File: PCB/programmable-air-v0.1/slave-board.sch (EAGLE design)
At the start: 16 parts, among them Q1 600mA/40V, Q2 600mA/40V, Q3 600mA/40V

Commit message: Forgot to add 5V input to slave boards
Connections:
- net GND: no longer U$5.P$2, U$6.P$2, U$7.P$2
- net N$7: now also U$7.P$2; no longer U$7.P$1
- net N$8: now also U$6.P$2; no longer U$6.P$1
- net N$9: now also U$5.P$2; no longer U$5.P$1
- net VIN: now also U$5.P$1, U$6.P$1, U$7.P$1
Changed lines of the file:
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@@
 <instance part="R2" gate="G$1" x="-11.43" y="-16.51"/>
 <instance part="R3" gate="G$1" x="21.59" y="-16.51"/>
-<instance part="U$5" gate="G$1" x="-29.21" y="-16.51" rot="R90"/>
-<instance part="U$6" gate="G$1" x="3.81" y="-16.51" rot="R90"/>
-<instance part="U$7" gate="G$1" x="36.83" y="-16.51" rot="R90"/>
+<instance part="U$5" gate="G$1" x="-33.02" y="-6.35" rot="R180"/>
+<instance part="U$6" gate="G$1" x="0" y="-6.35" rot="R180"/>
+<instance part="U$7" gate="G$1" x="33.02" y="-7.62" rot="R180"/>
 <instance part="SUPPLY1" gate="G$1" x="-48.26" y="35.56"/>
 <instance part="GND1" gate="1" x="13.97" y="-24.13"/>
@@
 <net name="N$7" class="0">
 <segment>
-<pinref part="U$7" gate="G$1" pin="P$1"/>
 <pinref part="Q3" gate="G$1" pin="C"/>
-<wire x1="36.83" y1="-13.97" x2="36.83" y2="-11.43" width="0.1524" layer="91"/>
-<wire x1="36.83" y1="-11.43" x2="33.02" y2="-11.43" width="0.1524" layer="91"/>
-<wire x1="36.83" y1="-11.43" x2="48.26" y2="-11.43" width="0.1524" layer="91"/>
+<wire x1="33.02" y1="-11.43" x2="48.26" y2="-11.43" width="0.1524" layer="91"/>
 <pinref part="U$4" gate="G$1" pin="P$2"/>
 <wire x1="48.26" y1="-11.43" x2="48.26" y2="-10.16" width="0.1524" layer="91"/>
+<pinref part="U$7" gate="G$1" pin="P$2"/>
+<wire x1="35.56" y1="-7.62" x2="48.26" y2="-7.62" width="0.1524" layer="91"/>
+<wire x1="48.26" y1="-7.62" x2="48.26" y2="-10.16" width="0.1524" layer="91"/>
 </segment>
 </net>
 <net name="N$8" class="0">
 <segment>
-<pinref part="U$6" gate="G$1" pin="P$1"/>
-<wire x1="3.81" y1="-13.97" x2="3.81" y2="-11.43" width="0.1524" layer="91"/>
 <pinref part="Q2" gate="G$1" pin="C"/>
-<wire x1="3.81" y1="-11.43" x2="0" y2="-11.43" width="0.1524" layer="91"/>
-<wire x1="3.81" y1="-11.43" x2="15.24" y2="-11.43" width="0.1524" layer="91"/>
+<wire x1="0" y1="-11.43" x2="15.24" y2="-11.43" width="0.1524" layer="91"/>
 <pinref part="U$3" gate="G$1" pin="P$2"/>
 <wire x1="15.24" y1="-11.43" x2="15.24" y2="-10.16" width="0.1524" layer="91"/>
+<pinref part="U$6" gate="G$1" pin="P$2"/>
+<wire x1="2.54" y1="-6.35" x2="15.24" y2="-6.35" width="0.1524" layer="91"/>
+<wire x1="15.24" y1="-6.35" x2="15.24" y2="-10.16" width="0.1524" layer="91"/>
 </segment>
 </net>
@@
 <segment>
 <pinref part="Q1" gate="G$1" pin="C"/>
-<wire x1="-33.02" y1="-11.43" x2="-29.21" y2="-11.43" width="0.1524" layer="91"/>
-<pinref part="U$5" gate="G$1" pin="P$1"/>
-<wire x1="-29.21" y1="-11.43" x2="-29.21" y2="-13.97" width="0.1524" layer="91"/>
 <pinref part="U$2" gate="G$1" pin="P$2"/>
 <wire x1="-17.78" y1="-10.16" x2="-17.78" y2="-11.43" width="0.1524" layer="91"/>
-<wire x1="-17.78" y1="-11.43" x2="-29.21" y2="-11.43" width="0.1524" layer="91"/>
+<wire x1="-17.78" y1="-11.43" x2="-33.02" y2="-11.43" width="0.1524" layer="91"/>
+<pinref part="U$5" gate="G$1" pin="P$2"/>
+<wire x1="-30.48" y1="-6.35" x2="-17.78" y2="-6.35" width="0.1524" layer="91"/>
+<wire x1="-17.78" y1="-6.35" x2="-17.78" y2="-10.16" width="0.1524" layer="91"/>
 </segment>
 </net>
@@
 <wire x1="-15.24" y1="-8.89" x2="17.78" y2="-8.89" width="0.1524" layer="91"/>
 <wire x1="17.78" y1="-8.89" x2="17.78" y2="-10.16" width="0.1524" layer="91"/>
-<wire x1="-48.26" y1="35.56" x2="-48.26" y2="-8.89" width="0.1524" layer="91"/>
+<wire x1="-48.26" y1="35.56" x2="-48.26" y2="-6.35" width="0.1524" layer="91"/>
 <pinref part="SUPPLY1" gate="G$1" pin="VIN"/>
 <junction x="-48.26" y="35.56"/>
+<pinref part="U$5" gate="G$1" pin="P$1"/>
+<wire x1="-48.26" y1="-6.35" x2="-48.26" y2="-8.89" width="0.1524" layer="91"/>
+<wire x1="-48.26" y1="-6.35" x2="-35.56" y2="-6.35" width="0.1524" layer="91"/>
+<wire x1="-15.24" y1="-8.89" x2="-15.24" y2="-6.35" width="0.1524" layer="91"/>
+<pinref part="U$6" gate="G$1" pin="P$1"/>
+<wire x1="-15.24" y1="-6.35" x2="-2.54" y2="-6.35" width="0.1524" layer="91"/>
+<wire x1="17.78" y1="-8.89" x2="17.78" y2="-7.62" width="0.1524" layer="91"/>
+<pinref part="U$7" gate="G$1" pin="P$1"/>
+<wire x1="17.78" y1="-7.62" x2="30.48" y2="-7.62" width="0.1524" layer="91"/>
 </segment>
 <segment>
@@
 <segment>
 <pinref part="Q3" gate="G$1" pin="E"/>
-<pinref part="U$7" gate="G$1" pin="P$2"/>
 <wire x1="33.02" y1="-21.59" x2="36.83" y2="-21.59" width="0.1524" layer="91"/>
-<wire x1="36.83" y1="-21.59" x2="36.83" y2="-19.05" width="0.1524" layer="91"/>
 <pinref part="Q2" gate="G$1" pin="E"/>
-<pinref part="U$6" gate="G$1" pin="P$2"/>
-<wire x1="3.81" y1="-21.59" x2="3.81" y2="-19.05" width="0.1524" layer="91"/>
 <wire x1="33.02" y1="-21.59" x2="13.97" y2="-21.59" width="0.1524" layer="91"/>
-<wire x1="13.97" y1="-21.59" x2="3.81" y2="-21.59" width="0.1524" layer="91"/>
-<wire x1="3.81" y1="-21.59" x2="0" y2="-21.59" width="0.1524" layer="91"/>
+<wire x1="13.97" y1="-21.59" x2="0" y2="-21.59" width="0.1524" layer="91"/>
 <pinref part="Q1" gate="G$1" pin="E"/>
-<pinref part="U$5" gate="G$1" pin="P$2"/>
-<wire x1="-33.02" y1="-21.59" x2="-29.21" y2="-21.59" width="0.1524" layer="91"/>
-<wire x1="-29.21" y1="-21.59" x2="-29.21" y2="-19.05" width="0.1524" layer="91"/>
-<wire x1="0" y1="-21.59" x2="-29.21" y2="-21.59" width="0.1524" layer="91"/>
+<wire x1="0" y1="-21.59" x2="-33.02" y2="-21.59" width="0.1524" layer="91"/>
 <pinref part="GND1" gate="1" pin="GND"/>
 <junction x="13.97" y="-21.59"/>

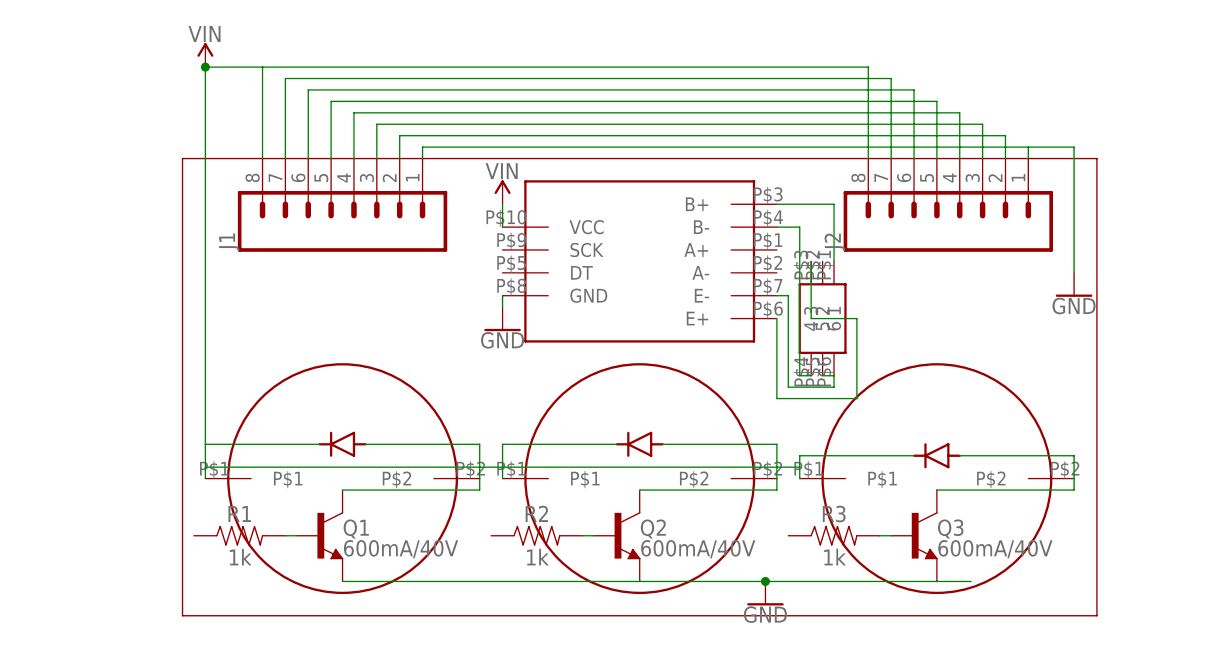
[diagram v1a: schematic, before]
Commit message: Fixed errors found after production, assembly and testing
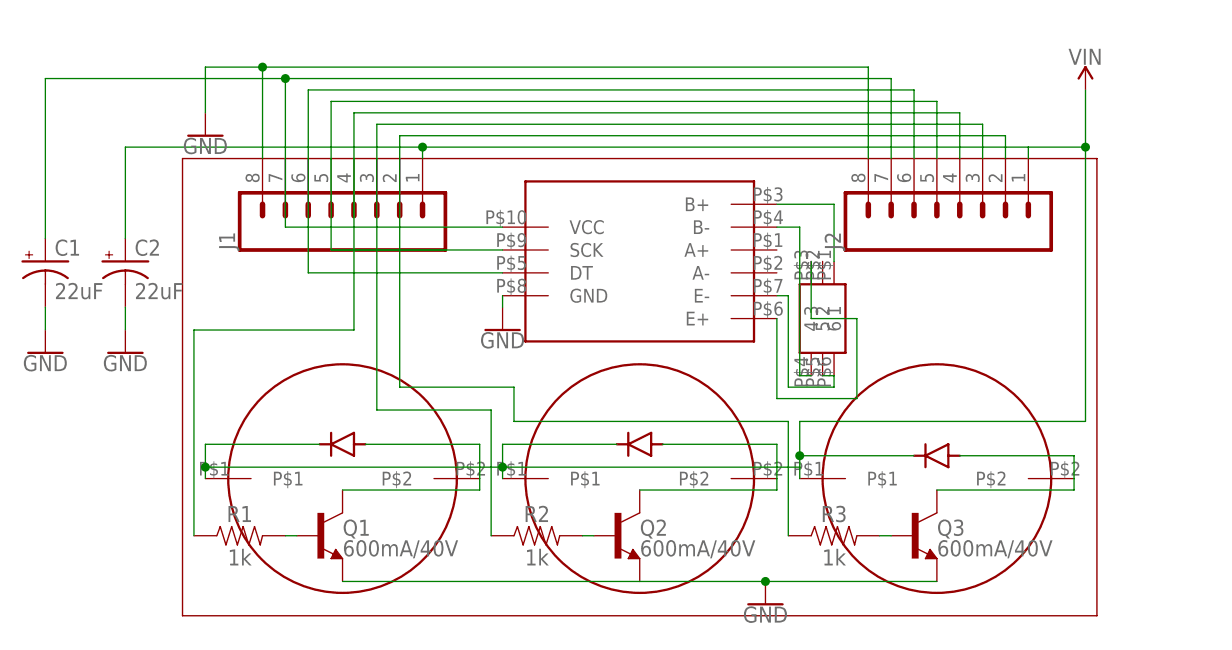
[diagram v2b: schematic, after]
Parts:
- added C1, C2: 22uF, SparkFun-Capacitors:22UF-POLAR-PANASONIC_C-35V-20%
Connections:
- net GND: now also C1.-, C2.-, J1.8, J2.8; no longer J1.1, J2.1
- net N$10: now also R2.1
- net N$12: now also R1.1
- net N$13: now also U$1.SCK
- net N$14: now also U$1.DT
- net N$15: now also C1.+, U$1.VCC
- net N$5: now also R3.1
- net VIN: now also C2.+, J1.1, J2.1; no longer J1.8, J2.8, U$1.VCC
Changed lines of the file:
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@@
 <setting verticaltext="up"/>
 </settings>
-<grid distance="0.05" unitdist="inch" unit="inch" style="lines" multiple="1" display="yes" altdistance="0.01" altunitdist="inch" altunit="inch"/>
+<grid distance="0.05" unitdist="inch" unit="inch" style="lines" multiple="1" display="no" altdistance="0.01" altunitdist="inch" altunit="inch"/>
 <layers>
 <layer number="1" name="Top" color="4" fill="1" visible="no" active="no"/>
@@
 <part name="GND2" library="SparkFun-PowerSymbols" deviceset="GND" device=""/>
 <part name="GND3" library="SparkFun-PowerSymbols" deviceset="GND" device=""/>
-<part name="SUPPLY2" library="SparkFun-PowerSymbols" deviceset="VIN" device=""/>
 <part name="U$8" library="programmable-air-components" deviceset="2SMPP-03" device=""/>
+<part name="C1" library="SparkFun-Capacitors" deviceset="22UF-POLAR" device="-PANASONIC_C-35V-20%" value="22uF"/>
+<part name="C2" library="SparkFun-Capacitors" deviceset="22UF-POLAR" device="-PANASONIC_C-35V-20%" value="22uF"/>
+<part name="GND4" library="SparkFun-PowerSymbols" deviceset="GND" device=""/>
+<part name="GND5" library="SparkFun-PowerSymbols" deviceset="GND" device=""/>
 </parts>
 <sheets>
@@
 <instance part="U$6" gate="G$1" x="0" y="-6.35" rot="R180"/>
 <instance part="U$7" gate="G$1" x="33.02" y="-7.62" rot="R180"/>
-<instance part="SUPPLY1" gate="G$1" x="-48.26" y="35.56"/>
+<instance part="SUPPLY1" gate="G$1" x="49.53" y="33.02"/>
 <instance part="GND1" gate="1" x="13.97" y="-24.13"/>
-<instance part="GND2" gate="1" x="48.26" y="10.16"/>
+<instance part="GND2" gate="1" x="-48.26" y="27.94"/>
 <instance part="GND3" gate="1" x="-15.24" y="6.35"/>
-<instance part="SUPPLY2" gate="G$1" x="-15.24" y="20.32"/>
 <instance part="U$8" gate="G$1" x="20.32" y="7.62" rot="R270"/>
+<instance part="C1" gate="G$1" x="-66.04" y="13.97"/>
+<instance part="C2" gate="G$1" x="-57.15" y="13.97"/>
+<instance part="GND4" gate="1" x="-66.04" y="3.81"/>
+<instance part="GND5" gate="1" x="-57.15" y="3.81"/>
 </instances>
 <busses>
@@
 <pinref part="J1" gate="G$1" pin="2"/>
 <wire x1="-26.67" y1="27.94" x2="-26.67" y2="25.4" width="0.1524" layer="91"/>
+<pinref part="R3" gate="G$1" pin="1"/>
+<wire x1="16.51" y1="-16.51" x2="16.51" y2="-3.81" width="0.1524" layer="91"/>
+<wire x1="16.51" y1="-3.81" x2="-13.97" y2="-3.81" width="0.1524" layer="91"/>
+<wire x1="-13.97" y1="-3.81" x2="-13.97" y2="0" width="0.1524" layer="91"/>
+<wire x1="-13.97" y1="0" x2="-26.67" y2="0" width="0.1524" layer="91"/>
+<wire x1="-26.67" y1="0" x2="-26.67" y2="25.4" width="0.1524" layer="91"/>
 </segment>
 </net>
@@
 <pinref part="J2" gate="G$1" pin="3"/>
 <wire x1="38.1" y1="29.21" x2="38.1" y2="25.4" width="0.1524" layer="91"/>
+<wire x1="-29.21" y1="25.4" x2="-29.21" y2="-2.54" width="0.1524" layer="91"/>
+<wire x1="-29.21" y1="-2.54" x2="-16.51" y2="-2.54" width="0.1524" layer="91"/>
+<pinref part="R2" gate="G$1" pin="1"/>
+<wire x1="-16.51" y1="-2.54" x2="-16.51" y2="-16.51" width="0.1524" layer="91"/>
 </segment>
 </net>
@@
 <pinref part="J1" gate="G$1" pin="4"/>
 <wire x1="-31.75" y1="30.48" x2="-31.75" y2="25.4" width="0.1524" layer="91"/>
+<pinref part="R1" gate="G$1" pin="1"/>
+<wire x1="-49.53" y1="-16.51" x2="-49.53" y2="6.35" width="0.1524" layer="91"/>
+<wire x1="-49.53" y1="6.35" x2="-31.75" y2="6.35" width="0.1524" layer="91"/>
+<wire x1="-31.75" y1="6.35" x2="-31.75" y2="25.4" width="0.1524" layer="91"/>
 </segment>
 </net>
@@
 <pinref part="J2" gate="G$1" pin="5"/>
 <wire x1="33.02" y1="31.75" x2="33.02" y2="25.4" width="0.1524" layer="91"/>
+<pinref part="U$1" gate="G$1" pin="SCK"/>
+<wire x1="-34.29" y1="25.4" x2="-34.29" y2="15.24" width="0.1524" layer="91"/>
+<wire x1="-34.29" y1="15.24" x2="-15.24" y2="15.24" width="0.1524" layer="91"/>
 </segment>
 </net>
@@
 <pinref part="J1" gate="G$1" pin="6"/>
 <wire x1="-36.83" y1="33.02" x2="-36.83" y2="25.4" width="0.1524" layer="91"/>
+<pinref part="U$1" gate="G$1" pin="DT"/>
+<wire x1="-15.24" y1="12.7" x2="-36.83" y2="12.7" width="0.1524" layer="91"/>
+<wire x1="-36.83" y1="12.7" x2="-36.83" y2="25.4" width="0.1524" layer="91"/>
 </segment>
 </net>
@@
 <pinref part="J2" gate="G$1" pin="7"/>
 <wire x1="27.94" y1="34.29" x2="27.94" y2="25.4" width="0.1524" layer="91"/>
+<pinref part="U$1" gate="G$1" pin="VCC"/>
+<wire x1="-39.37" y1="25.4" x2="-39.37" y2="17.78" width="0.1524" layer="91"/>
+<wire x1="-39.37" y1="17.78" x2="-15.24" y2="17.78" width="0.1524" layer="91"/>
+<pinref part="C1" gate="G$1" pin="+"/>
+<wire x1="-39.37" y1="34.29" x2="-66.04" y2="34.29" width="0.1524" layer="91"/>
+<wire x1="-66.04" y1="34.29" x2="-66.04" y2="16.51" width="0.1524" layer="91"/>
+<junction x="-39.37" y="34.29"/>
 </segment>
 </net>
 <net name="VIN" class="0">
 <segment>
-<pinref part="J2" gate="G$1" pin="8"/>
-<wire x1="25.4" y1="25.4" x2="25.4" y2="35.56" width="0.1524" layer="91"/>
-<wire x1="25.4" y1="35.56" x2="-41.91" y2="35.56" width="0.1524" layer="91"/>
-<pinref part="J1" gate="G$1" pin="8"/>
-<wire x1="-41.91" y1="35.56" x2="-41.91" y2="25.4" width="0.1524" layer="91"/>
-<wire x1="-41.91" y1="35.56" x2="-48.26" y2="35.56" width="0.1524" layer="91"/>
+<pinref part="J1" gate="G$1" pin="1"/>
+<wire x1="-24.13" y1="25.4" x2="-24.13" y2="26.67" width="0.1524" layer="91"/>
+<pinref part="J2" gate="G$1" pin="1"/>
+<wire x1="-24.13" y1="26.67" x2="43.18" y2="26.67" width="0.1524" layer="91"/>
+<wire x1="43.18" y1="26.67" x2="43.18" y2="25.4" width="0.1524" layer="91"/>
+<pinref part="SUPPLY1" gate="G$1" pin="VIN"/>
+<wire x1="43.18" y1="26.67" x2="49.53" y2="26.67" width="0.1524" layer="91"/>
+<wire x1="49.53" y1="26.67" x2="49.53" y2="33.02" width="0.1524" layer="91"/>
 <pinref part="U$2" gate="G$1" pin="P$1"/>
 <wire x1="-48.26" y1="-10.16" x2="-48.26" y2="-8.89" width="0.1524" layer="91"/>
@@
 <wire x1="-15.24" y1="-8.89" x2="17.78" y2="-8.89" width="0.1524" layer="91"/>
 <wire x1="17.78" y1="-8.89" x2="17.78" y2="-10.16" width="0.1524" layer="91"/>
-<wire x1="-48.26" y1="35.56" x2="-48.26" y2="-6.35" width="0.1524" layer="91"/>
-<pinref part="SUPPLY1" gate="G$1" pin="VIN"/>
-<junction x="-48.26" y="35.56"/>
 <pinref part="U$5" gate="G$1" pin="P$1"/>
 <wire x1="-48.26" y1="-6.35" x2="-48.26" y2="-8.89" width="0.1524" layer="91"/>
@@
 <pinref part="U$7" gate="G$1" pin="P$1"/>
 <wire x1="17.78" y1="-7.62" x2="30.48" y2="-7.62" width="0.1524" layer="91"/>
-</segment>
-<segment>
-<pinref part="SUPPLY2" gate="G$1" pin="VIN"/>
-<pinref part="U$1" gate="G$1" pin="VCC"/>
-<wire x1="-15.24" y1="20.32" x2="-15.24" y2="17.78" width="0.1524" layer="91"/>
+<wire x1="17.78" y1="-7.62" x2="17.78" y2="-3.81" width="0.1524" layer="91"/>
+<wire x1="17.78" y1="-3.81" x2="49.53" y2="-3.81" width="0.1524" layer="91"/>
+<wire x1="49.53" y1="-3.81" x2="49.53" y2="26.67" width="0.1524" layer="91"/>
+<pinref part="C2" gate="G$1" pin="+"/>
+<wire x1="-57.15" y1="16.51" x2="-57.15" y2="26.67" width="0.1524" layer="91"/>
+<wire x1="-57.15" y1="26.67" x2="-24.13" y2="26.67" width="0.1524" layer="91"/>
+<junction x="-24.13" y="26.67"/>
+<junction x="49.53" y="26.67"/>
+<junction x="-48.26" y="-8.89"/>
+<junction x="17.78" y="-7.62"/>
+<junction x="-15.24" y="-8.89"/>
 </segment>
 </net>
@@
 <segment>
 <pinref part="Q3" gate="G$1" pin="E"/>
-<wire x1="33.02" y1="-21.59" x2="36.83" y2="-21.59" width="0.1524" layer="91"/>
 <pinref part="Q2" gate="G$1" pin="E"/>
 <wire x1="33.02" y1="-21.59" x2="13.97" y2="-21.59" width="0.1524" layer="91"/>
@@
 </segment>
 <segment>
-<pinref part="J1" gate="G$1" pin="1"/>
-<wire x1="-24.13" y1="25.4" x2="-24.13" y2="26.67" width="0.1524" layer="91"/>
-<pinref part="J2" gate="G$1" pin="1"/>
-<wire x1="-24.13" y1="26.67" x2="43.18" y2="26.67" width="0.1524" layer="91"/>
-<wire x1="43.18" y1="26.67" x2="43.18" y2="25.4" width="0.1524" layer="91"/>
-<wire x1="43.18" y1="26.67" x2="48.26" y2="26.67" width="0.1524" layer="91"/>
-<pinref part="GND2" gate="1" pin="GND"/>
-<wire x1="48.26" y1="26.67" x2="48.26" y2="12.7" width="0.1524" layer="91"/>
-</segment>
-<segment>
 <pinref part="U$1" gate="G$1" pin="GND"/>
 <pinref part="GND3" gate="1" pin="GND"/>
 <wire x1="-15.24" y1="10.16" x2="-15.24" y2="8.89" width="0.1524" layer="91"/>
 </segment>
-</net>
+<segment>
+<pinref part="GND2" gate="1" pin="GND"/>
+<wire x1="-48.26" y1="30.48" x2="-48.26" y2="35.56" width="0.1524" layer="91"/>
+<wire x1="-48.26" y1="35.56" x2="-41.91" y2="35.56" width="0.1524" layer="91"/>
+<pinref part="J1" gate="G$1" pin="8"/>
+<pinref part="J2" gate="G$1" pin="8"/>
+<wire x1="25.4" y1="25.4" x2="25.4" y2="35.56" width="0.1524" layer="91"/>
+<wire x1="25.4" y1="35.56" x2="-41.91" y2="35.56" width="0.1524" layer="91"/>
+<wire x1="-41.91" y1="35.56" x2="-41.91" y2="25.4" width="0.1524" layer="91"/>
+<junction x="-41.91" y="35.56"/>
+</segment>
+<segment>
+<pinref part="C2" gate="G$1" pin="-"/>
+<pinref part="GND5" gate="1" pin="GND"/>
+<wire x1="-57.15" y1="8.89" x2="-57.15" y2="6.35" width="0.1524" layer="91"/>
+</segment>
+<segment>
+<pinref part="C1" gate="G$1" pin="-"/>
+<pinref part="GND4" gate="1" pin="GND"/>
+<wire x1="-66.04" y1="8.89" x2="-66.04" y2="6.35" width="0.1524" layer="91"/>
+</segment>
+</net>
